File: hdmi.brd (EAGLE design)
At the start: 160 x 100 mm, 156 parts, among them IC1 FT2232HL, U0 6SLX45CSG324, U1 MT41J64M16, U2 TPD12S016RKTR, U3 TPD12S016RKTR, U4 TPD12S016RKTR, U5 MNR18, U6 MNR18, U8 20Mhz

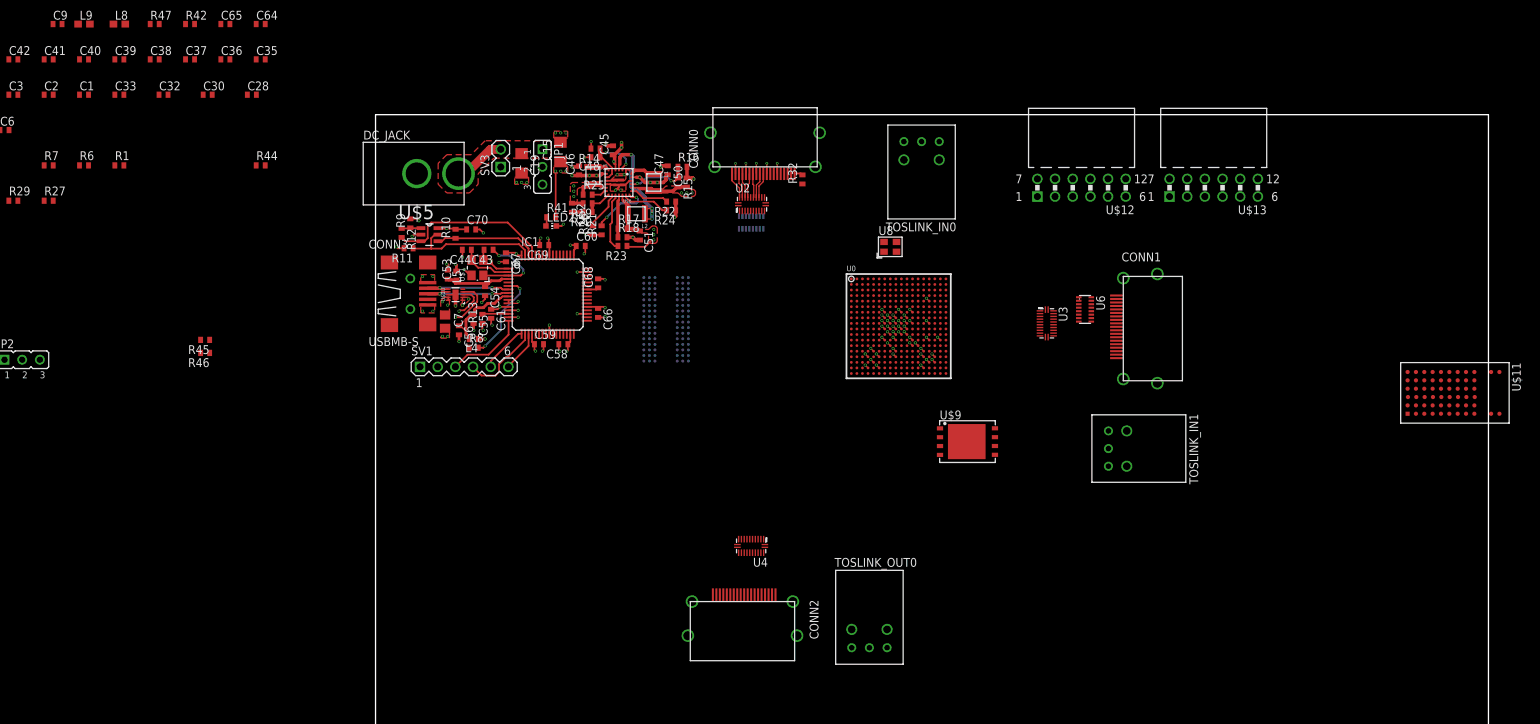
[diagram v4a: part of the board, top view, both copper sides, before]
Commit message: Switched HDMI companion chip package, finished routing of the first HDMI group
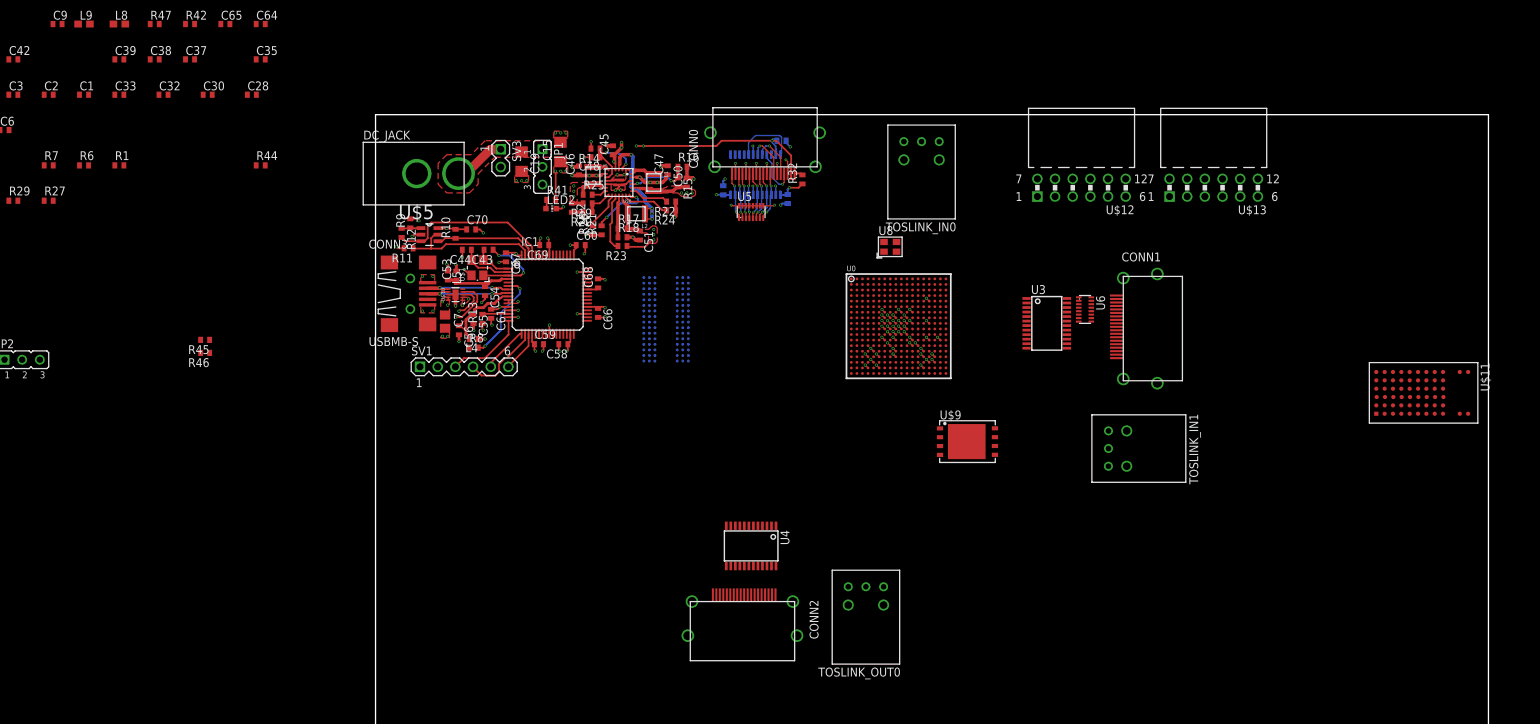
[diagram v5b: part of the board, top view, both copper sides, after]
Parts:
- U2, U3, U4: value TPD12S016RKTR -> TPD12S016PWR; device prj-hdmi:UQFN24 -> prj-hdmi:PW_R-PDSO-G24
- moved C41 106.0 mm to (58.4, 96.2), flipped to the bottom, turned to 180 degrees
- moved C40 93.8 mm to (50.0, 89.1), flipped to the bottom, turned to 90 degrees
- moved C36 83.3 mm to (59.2, 87.9), flipped to the bottom, turned to 270 degrees
- moved U$11 4.50 mm to (150.5, 60.0)
- moved U2 4.28 mm to (54.6, 91.4), flipped to the bottom, turned to 180 degrees
- moved TOSLINK_OUT0 3.54 mm to (70.5, 29.5), turned to 180 degrees
- moved LED2 2.50 mm to (25.2, 86.5)
- moved R41 2.50 mm to (25.2, 87.8)
- moved U5 1.50 mm to (54.0, 86.0), flipped to the top, turned to 0 degrees
- moved C19 0.25 mm to (21.0, 93.2)
- moved C60 0.12 mm to (29.5, 81.2)
- moved L5 0.12 mm to (10.4, 76.9)
- turned SV3 to 270 degrees
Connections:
- net +3V3: now also U2.24, U3.24, U4.24; no longer U2.23, U3.23, U4.23
- net +5V: now also U2.11, U3.11, U4.11; no longer U2.10, U3.10, U4.10
- net CENTER: now also SV3.1; no longer SV3.2
- net GND: now also SV3.2, U2.14, U2.19, U2.6, U3.14, U3.19, U3.6, U4.14, U4.19, U4.6; no longer SV3.1, U2.13, U2.18, U2.5, U3.13, U3.18, U3.5, U4.13, U4.18, U4.5
- net HDMI_RX0_5V: now also U2.13; no longer U2.12
- net HDMI_RX0_CEC: now also U2.7; no longer U2.6
- net HDMI_RX0_CEC_3V3: now also U2.1; no longer U2.24
- net HDMI_RX0_CLK_N: now also U2.15; no longer U2.14
- net HDMI_RX0_CLK_P: now also U2.16; no longer U2.15
- net HDMI_RX0_CTRL_EN: now also U2.12, U2.5; no longer U2.11, U2.4
- net HDMI_RX0_DATA0_N: now also U2.17; no longer U2.16
- net HDMI_RX0_DATA0_P: now also U2.18; no longer U2.17
- net HDMI_RX0_DATA1_N: now also U2.20; no longer U2.19
- net HDMI_RX0_DATA1_P: now also U2.21; no longer U2.20
- net HDMI_RX0_DATA2_N: now also U2.22; no longer U2.21
- net HDMI_RX0_DATA2_P: now also U2.23; no longer U2.22
- net HDMI_RX0_SCL_3V3: now also U2.2; no longer U2.1
- net HDMI_RX0_SCL_5V: now also U2.8; no longer U2.7
- net HDMI_RX0_SDA_3V3: now also U2.3; no longer U2.2
- net HDMI_RX0_SDA_5V: now also U2.9; no longer U2.8
- net HDMI_RX1_5V: now also U3.13; no longer U3.12
- net HDMI_RX1_CEC: now also U3.7; no longer U3.6
- net HDMI_RX1_CEC_3V3: now also U3.1; no longer U3.24
- net HDMI_RX1_CLK_N: now also U3.15; no longer U3.14
- net HDMI_RX1_CLK_P: now also U3.16; no longer U3.15
- net HDMI_RX1_CTRL_EN: now also U3.12, U3.5; no longer U3.11, U3.4
- net HDMI_RX1_DATA0_N: now also U3.17; no longer U3.16
- net HDMI_RX1_DATA0_P: now also U3.18; no longer U3.17
- net HDMI_RX1_DATA1_N: now also U3.20; no longer U3.19
- net HDMI_RX1_DATA1_P: now also U3.21; no longer U3.20
- net HDMI_RX1_DATA2_N: now also U3.22; no longer U3.21
- net HDMI_RX1_DATA2_P: now also U3.23; no longer U3.22
- net HDMI_RX1_SCL_3V3: now also U3.2; no longer U3.1
- net HDMI_RX1_SCL_5V: now also U3.8; no longer U3.7
- net HDMI_RX1_SDA_3V3: now also U3.3; no longer U3.2
- net HDMI_RX1_SDA_5V: now also U3.9; no longer U3.8
- net HDMI_TX0_5V: now also U4.13; no longer U4.12
- net HDMI_TX0_CEC: now also U4.7; no longer U4.6
- net HDMI_TX0_CEC_3V3: now also U4.1; no longer U4.24
- net HDMI_TX0_CLK_N: now also U4.15; no longer U4.14
- net HDMI_TX0_CLK_P: now also U4.16; no longer U4.15
- net HDMI_TX0_CTRL_EN: now also U4.12, U4.5; no longer U4.11, U4.4
- net HDMI_TX0_DATA0_N: now also U4.17; no longer U4.16
- net HDMI_TX0_DATA0_P: now also U4.18; no longer U4.17
- net HDMI_TX0_DATA1_N: now also U4.20; no longer U4.19
- net HDMI_TX0_DATA1_P: now also U4.21; no longer U4.20
- net HDMI_TX0_DATA2_N: now also U4.22; no longer U4.21
- net HDMI_TX0_DATA2_P: now also U4.23; no longer U4.22
- net HDMI_TX0_HPD_3V3: now also U4.4; no longer U4.3
- net HDMI_TX0_HPD_5V: now also U4.10; no longer U4.9
- net HDMI_TX0_SCL_3V3: now also U4.2; no longer U4.1
- net HDMI_TX0_SCL_5V: now also U4.8; no longer U4.7
- net HDMI_TX0_SDA_3V3: now also U4.3; no longer U4.2
- net HDMI_TX0_SDA_5V: now also U4.9; no longer U4.8
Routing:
- net +5V: track 27.3 -> 51.0 mm, vias 14 -> 17
- net HDMI_RX0_CTRL_EN: track 0.00 -> 9.55 mm
- net +3V3: track 37.3 -> 45.8 mm, vias 25 -> 28
- net HDMI_RX0_SDA_5V: track 0.00 -> 7.15 mm, vias 0 -> 1
- net HDMI_RX0_CLK_N: track 0.00 -> 6.99 mm, vias 0 -> 2
- net HDMI_RX0_SCL_5V: track 0.00 -> 6.57 mm, vias 0 -> 1
- net GND: track 74.3 -> 80.8 mm, vias 70 -> 77
- net HDMI_RX0_CEC: track 0.00 -> 6.35 mm, vias 0 -> 1
- net HDMI_RX0_5V: track 0.00 -> 4.24 mm, vias 0 -> 1
- net HDMI_RX0_DATA0_P: track 3.52 -> 7.03 mm, vias 0 -> 2
- net HDMI_RX0_CLK_P: track 3.71 -> 7.07 mm, vias 0 -> 2
- net HDMI_RX0_DATA0_N: track 3.67 -> 6.98 mm, vias 0 -> 2
- net HDMI_RX0_DATA1_P: track 3.61 -> 6.66 mm, vias 0 -> 2
- net HDMI_RX0_DATA2_N: track 3.65 -> 6.68 mm, vias 0 -> 2
- net HDMI_RX0_DATA1_N: track 3.56 -> 6.55 mm, vias 0 -> 2
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- added copper zone on layer 16, net +5V

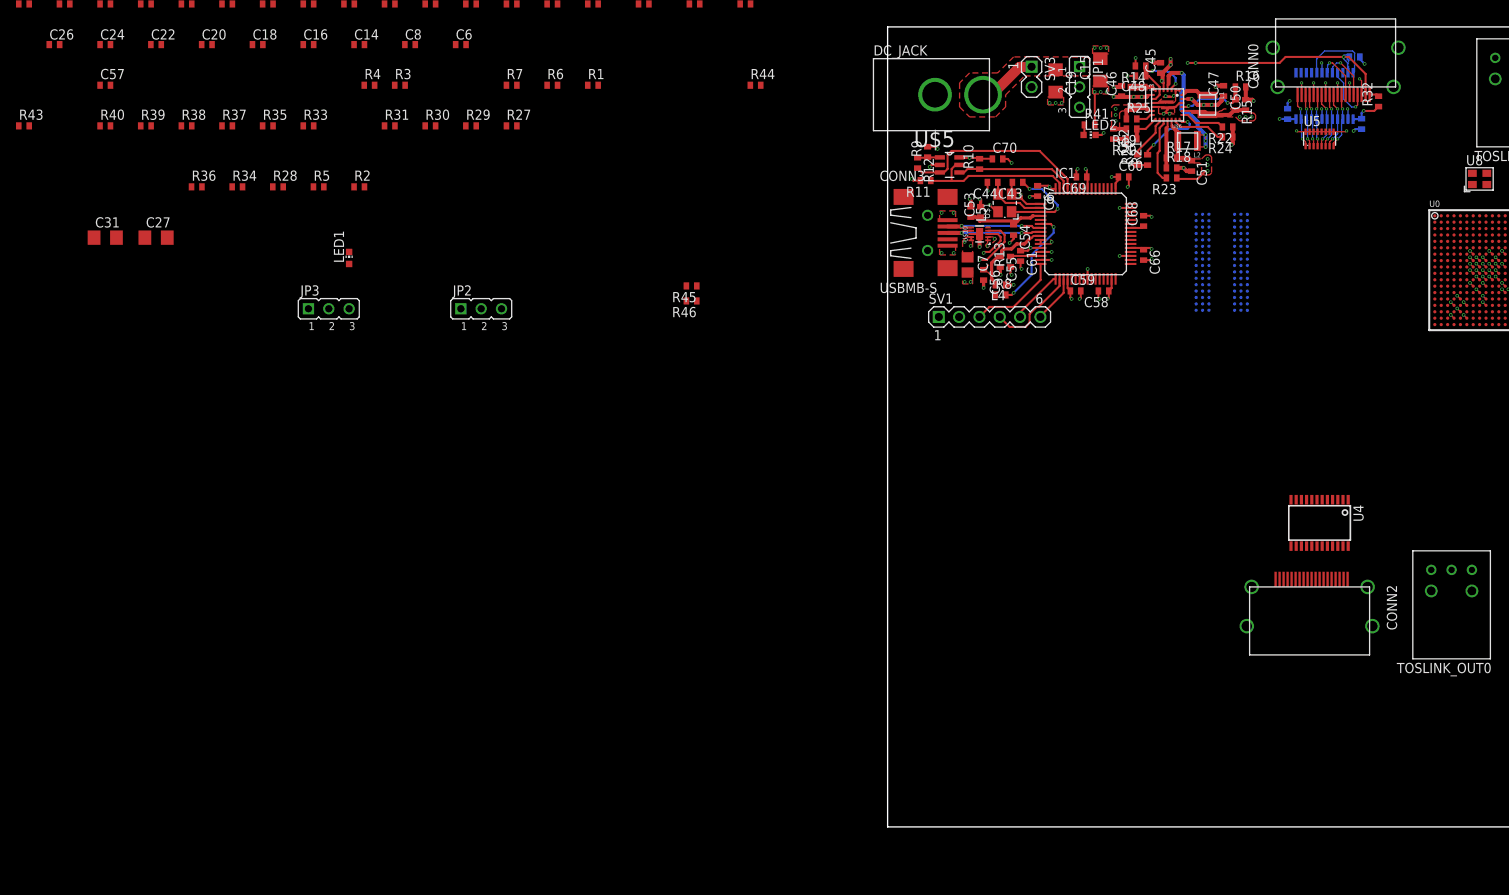
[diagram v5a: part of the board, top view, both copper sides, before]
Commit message: Switched all parts to the version of prj-hdmi.lbr; Corrected the "+5V" ping naming conflict; Exported BOM.xlsx
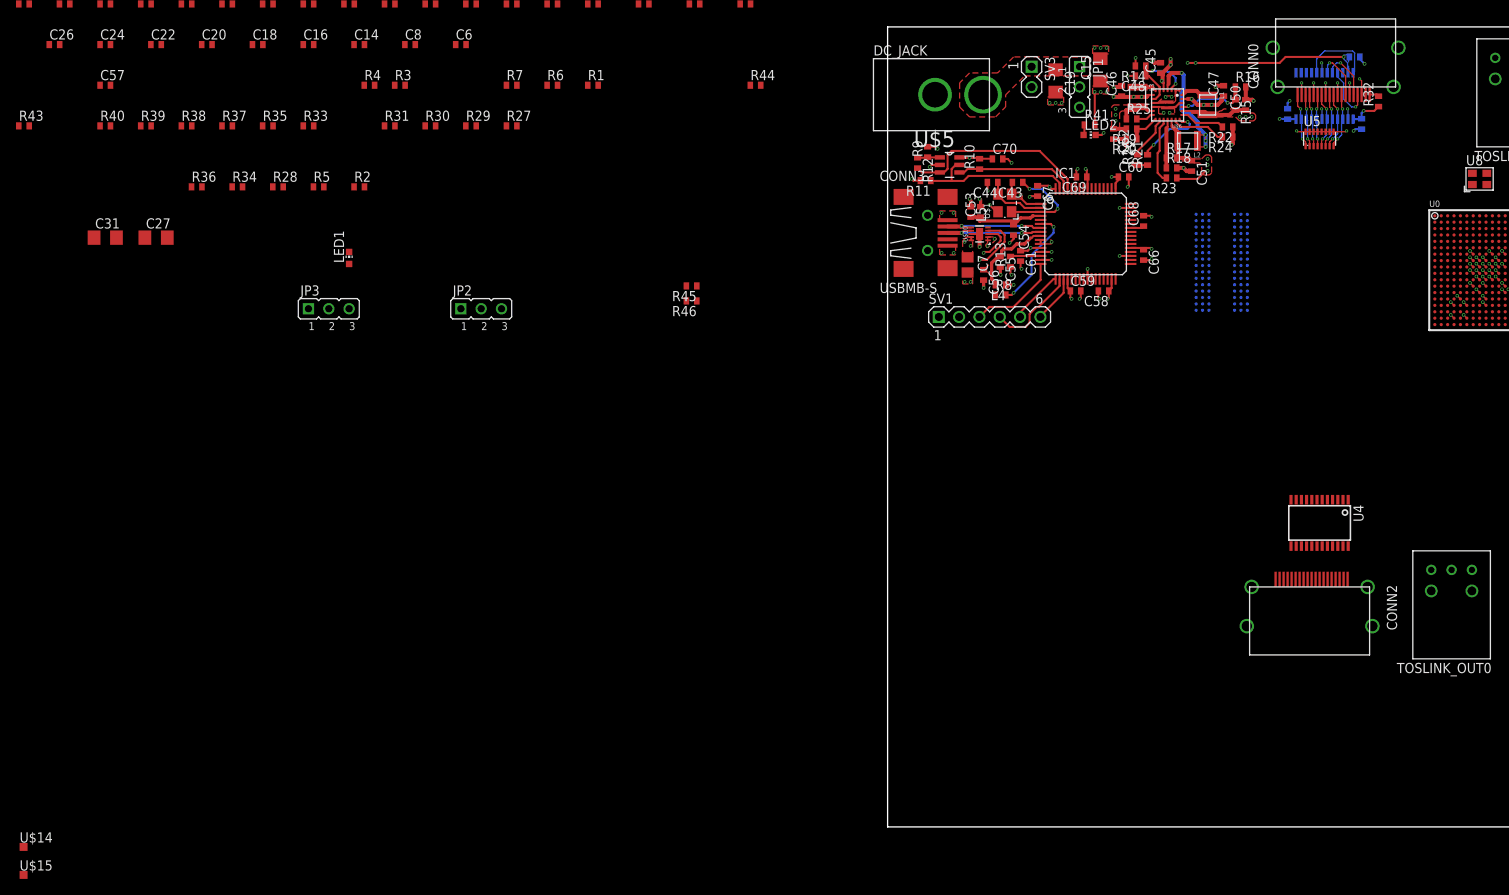
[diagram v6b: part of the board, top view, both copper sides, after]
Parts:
- added U$14, U$15: TP10SQ, prj-hdmi:TP10SQ
- C1, C10, C11, C12, C13, C14, C16, C17, C18, C2, C20, C21, C22, C24, C25, C26, C28, C29, C3, C30, C32, C33, C34, C35, C36, C37, C38, C39, C4, C40, C41, C42, C45, C46, C47, C48, C49, C5, C50, C51, C52, C6, C8, C9: device rcl:C0402 -> prj-hdmi:0402
- C15, C19, C27, C31: device rcl:C1206 -> prj-hdmi:C1206
- C43, C44, C53, C54, C55, C56, C57, C58, C59, C60, C61, C66, C67, C68, C69, C70: device resistor:C0402 -> prj-hdmi:0402
- C64, C65: value 0.1 -> 0.1u
- R1, R10, R11, R12, R13, R14, R15, R16, R17, R18, R19, R2, R20, R21, R22, R23, R24, R25, R26, R27, R28, R29, R3, R30, R31, R32, R33, R34, R35, R36, R37, R38, R39, R4, R40, R41, R43, R44, R45, R46, R5, R6, R7, R8, R9: device resistor:R0402 -> prj-hdmi:0402
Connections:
- removed net BT_SCL: U$11.E2, U0.V5
- removed net BT_SDA: U$11.E1, U0.U5
- new net +5V_SUPPLY: CONN0.18, CONN1.18
- new net N$19: U$11.E1, U$15.TP
- new net N$29: U$11.E2, U$14.TP
- net +5V: no longer CONN0.18, CONN1.18
- net BT_RESET#: now also U0.V5; no longer U0.T5
- net BT_WAKE: now also U0.U5; no longer U0.R5
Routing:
- net CENTER: track 7.52 -> 0.00 mm
- net +5V: track 51.0 -> 44.7 mm
- net GND: track 80.8 -> 77.8 mm
- net BT_RESET#: track 0.57 -> 0.00 mm, vias 1 -> 0
